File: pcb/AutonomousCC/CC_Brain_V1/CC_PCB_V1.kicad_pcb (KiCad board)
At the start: 2 copper layers, 104.2 x 144.9 mm, 14 parts, among them J1 Screw_Terminal_01x07, J2 Antenna_Conn_02x04_Odd_Even, J3 USB1130-15-A_REVA, J5 Relay_Conn_01x06, U1 Pico, U2 LM337_TO3

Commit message: Added Switch for Pico Programming
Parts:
- added S1: SSA12G, my_footprints:SW_SSA12G, F.Cu at (118.1, 27.9)
- J2: footprint Connector_PinHeader_2.00mm:PinHeader_2x04_P2.00mm_Vertical -> Connector_PinHeader_2.54mm:PinHeader_2x04_P2.54mm_Vertical
- J5: footprint Connector_PinHeader_2.00mm:PinHeader_1x06_P2.00mm_Vertical -> Connector_PinHeader_2.54mm:PinHeader_1x06_P2.54mm_Vertical
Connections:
- U1 pad 39: +3.3V -> +3.3V_Pico
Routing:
- net +3.3V_Pico: track 0.00 -> 30.9 mm
- net +3.3V: track 202.9 -> 190.9 mm
- removed copper zone on B.Cu, net GND
- removed copper zone on F.Cu, net GND

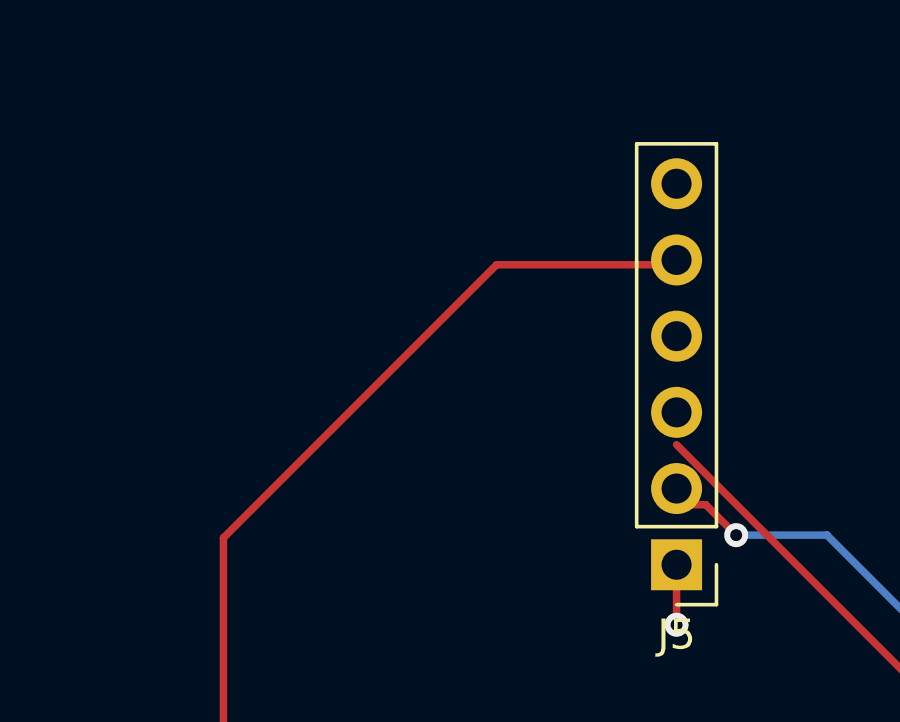
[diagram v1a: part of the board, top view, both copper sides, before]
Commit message: Updated Antenna CC_Brain Pins and Added Relay Circuit
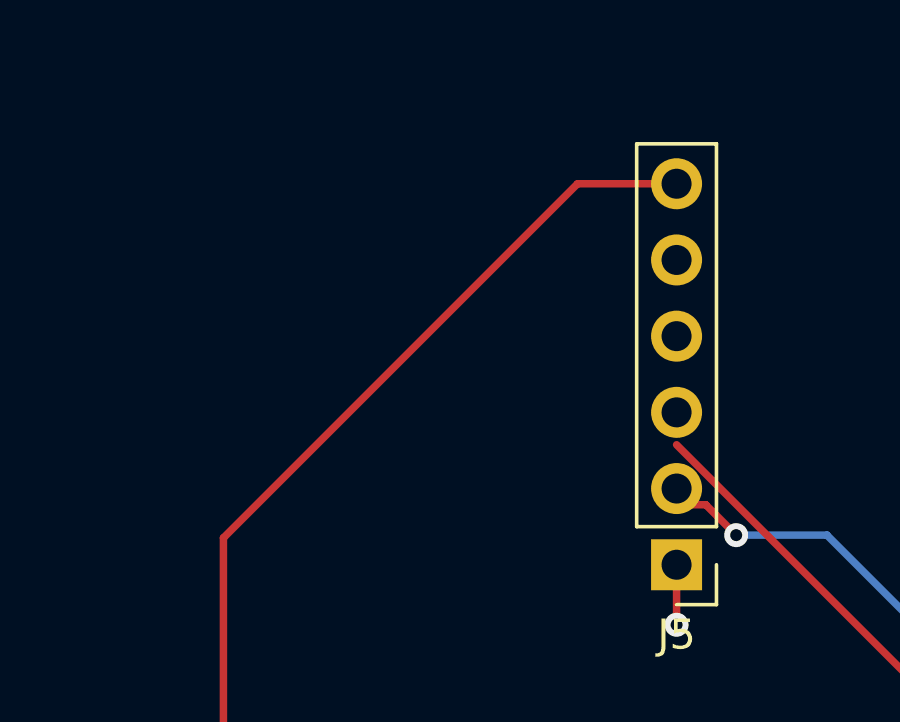
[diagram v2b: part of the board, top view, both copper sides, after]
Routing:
- net +5V: track 163.4 -> 164.6 mm

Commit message: Added most of the footprints
Still need Diodes, Resistors (if THT or SMD), and LED footprints
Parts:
- removed S1: SSA12G, my_footprints:SW_SSA12G
- added J4: Conn_01x02_Male, Connector_PinHeader_2.54mm:PinHeader_1x02_P2.54mm_Vertical, F.Cu at (234.3, 27.4)
- added J6: Conn_01x02_Male, Connector_PinHeader_2.54mm:PinHeader_1x02_P2.54mm_Vertical, F.Cu at (234.3, 34.6)
- added J7: Linear Actuator Power, MCU_RaspberryPi_and_Boards:TE_282837-2, F.Cu at (177.6, 57.9)
- added J8: Linear Actuator, MCU_RaspberryPi_and_Boards:TE_282837-2, F.Cu at (189.3, 57.9)
- added J9: Conn_01x02_Male, Connector_PinHeader_2.54mm:PinHeader_1x02_P2.54mm_Vertical, F.Cu at (245.8, 27.4)
- added K1: FINDER-40.11, Relay_THT:Relay_SPDT_Finder_40.11, F.Cu at (175.5, 29.2)
- added K2: FINDER-40.11, Relay_THT:Relay_SPDT_Finder_40.11, F.Cu at (205.6, 29.2)
- added Q1: PC817A, MCU_RaspberryPi_and_Boards:DIP762W50P254L650H458Q4B, F.Cu at (200.9, 56.3)
- added Q2: PC817A, MCU_RaspberryPi_and_Boards:DIP762W50P254L650H458Q4B, F.Cu at (211.9, 56.3)
- added Q3: BC547A, Package_TO_SOT_THT:TO-92_Inline, F.Cu at (219.1, 56.3)
- added Q4: BC547A, Package_TO_SOT_THT:TO-92_Inline, F.Cu at (234.0, 42.7)
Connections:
- J2 pad 6: GP4 -> GP7
- J2 pad 7: GP7 -> GP4

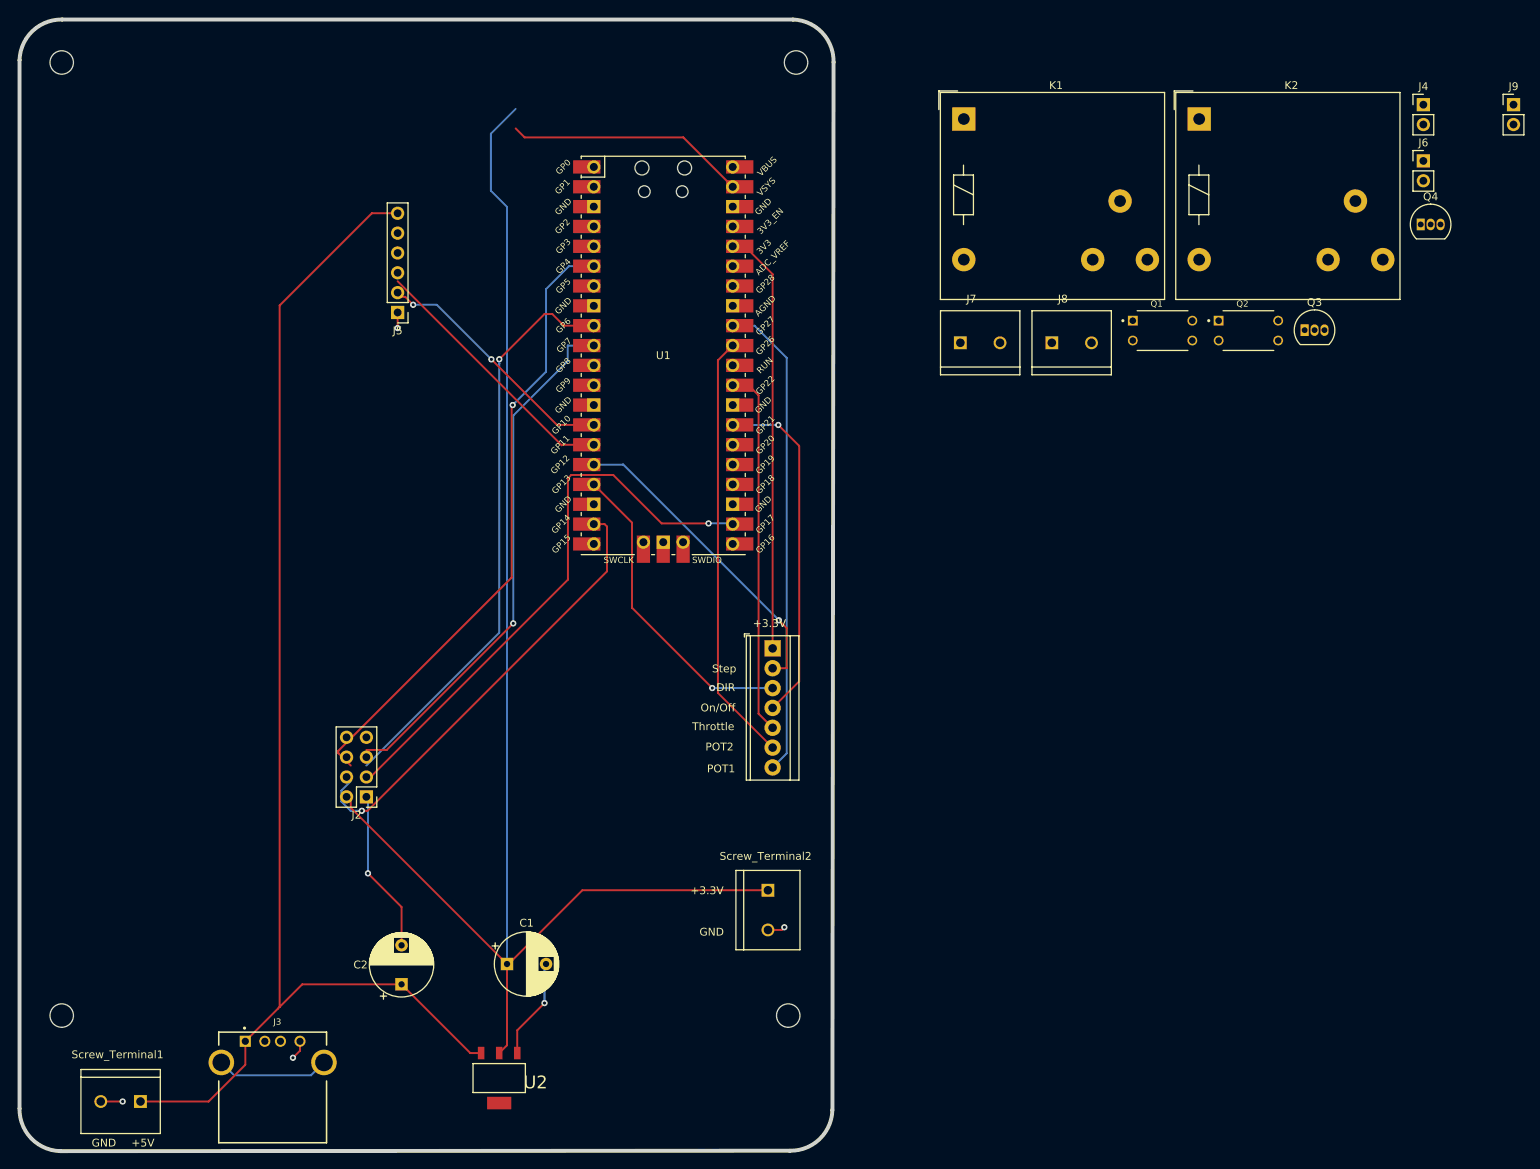
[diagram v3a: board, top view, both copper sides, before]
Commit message: Updated Footprints and PCB Layout
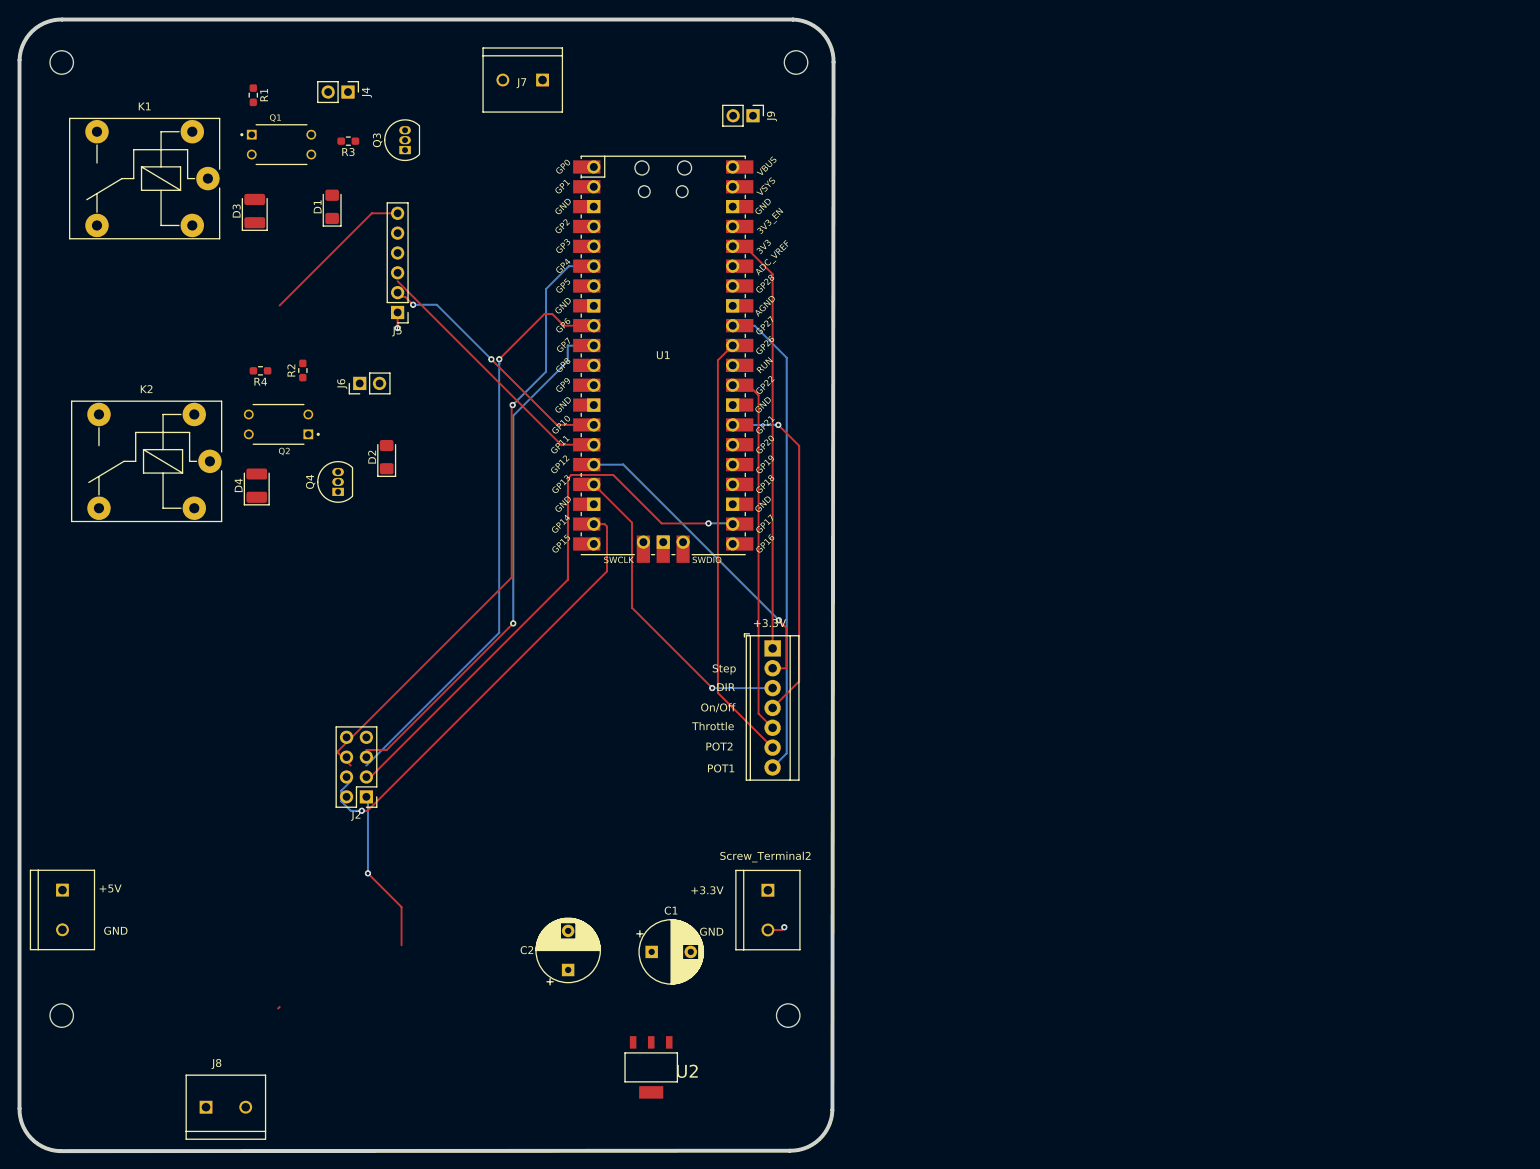
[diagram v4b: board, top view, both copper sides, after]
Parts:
- removed J3: USB1130-15-A_REVA, MCU_RaspberryPi_and_Boards:GCT_USB1130-15-A_REVA
- added D1: SMD LED1, LED_SMD:LED_1206_3216Metric_Pad1.42x1.75mm_HandSolder, F.Cu at (94.6, 40.5)
- added D2: SMD LED2, LED_SMD:LED_1206_3216Metric_Pad1.42x1.75mm_HandSolder, F.Cu at (101.6, 72.5)
- added D3: DIODE, Diode_SMD:D_1210_3225Metric_Pad1.42x2.65mm_HandSolder, F.Cu at (84.7, 41.0)
- added D4: DIODE, Diode_SMD:D_1210_3225Metric_Pad1.42x2.65mm_HandSolder, F.Cu at (85.0, 76.2)
- added R1: 1k, Resistor_SMD:R_0603_1608Metric_Pad0.98x0.95mm_HandSolder, F.Cu at (84.5, 26.2)
- added R2: 1k, Resistor_SMD:R_0603_1608Metric_Pad0.98x0.95mm_HandSolder, F.Cu at (90.9, 61.4)
- added R3: 1k, Resistor_SMD:R_0603_1608Metric_Pad0.98x0.95mm_HandSolder, F.Cu at (96.7, 32.1)
- added R4: 1k, Resistor_SMD:R_0603_1608Metric_Pad0.98x0.95mm_HandSolder, F.Cu at (85.4, 61.5)
- K1, K2: footprint Relay_THT:Relay_SPDT_Finder_40.11 -> Relay_THT:Relay_SPDT_Finder_36.11
- moved J8 145.9 mm to (81.0, 155.7)
- moved Q4 142.7 mm to (95.4, 77.0), turned to 90 degrees
- moved J6 139.1 mm to (98.1, 63.1), turned to 90 degrees
- moved J4 137.7 mm to (96.6, 25.8), turned to 270 degrees
- moved K2 134.0 mm to (79.0, 73.1), turned to 180 degrees
- moved Q2 124.7 mm to (87.8, 68.3), turned to 180 degrees
- moved Q3 117.4 mm to (103.9, 33.2), turned to 90 degrees
- moved Q1 115.3 mm to (88.1, 32.5)
- moved J9 97.4 mm to (148.5, 28.8), turned to 270 degrees
- moved K1 97.1 mm to (78.7, 36.9), turned to 180 degrees
- moved J7 67.5 mm to (119.0, 24.2), turned to 180 degrees
- moved Screw_Terminal1 25.6 mm to (60.1, 130.5), turned to 270 degrees
- moved C2 21.4 mm to (124.8, 138.2)
- moved U2 19.5 mm to (135.5, 150.6)
- moved C1 18.6 mm to (135.5, 135.9)
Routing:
- net +3.3V: track 190.9 -> 0.00 mm
- net +5V: track 164.6 -> 20.3 mm
- net +3.3V_Pico: track 30.9 -> 0.00 mm
- net GND: track 42.9 -> 25.1 mm, vias 6 -> 3
- net Net-(J3-PadS1): track 14.5 -> 0.00 mm

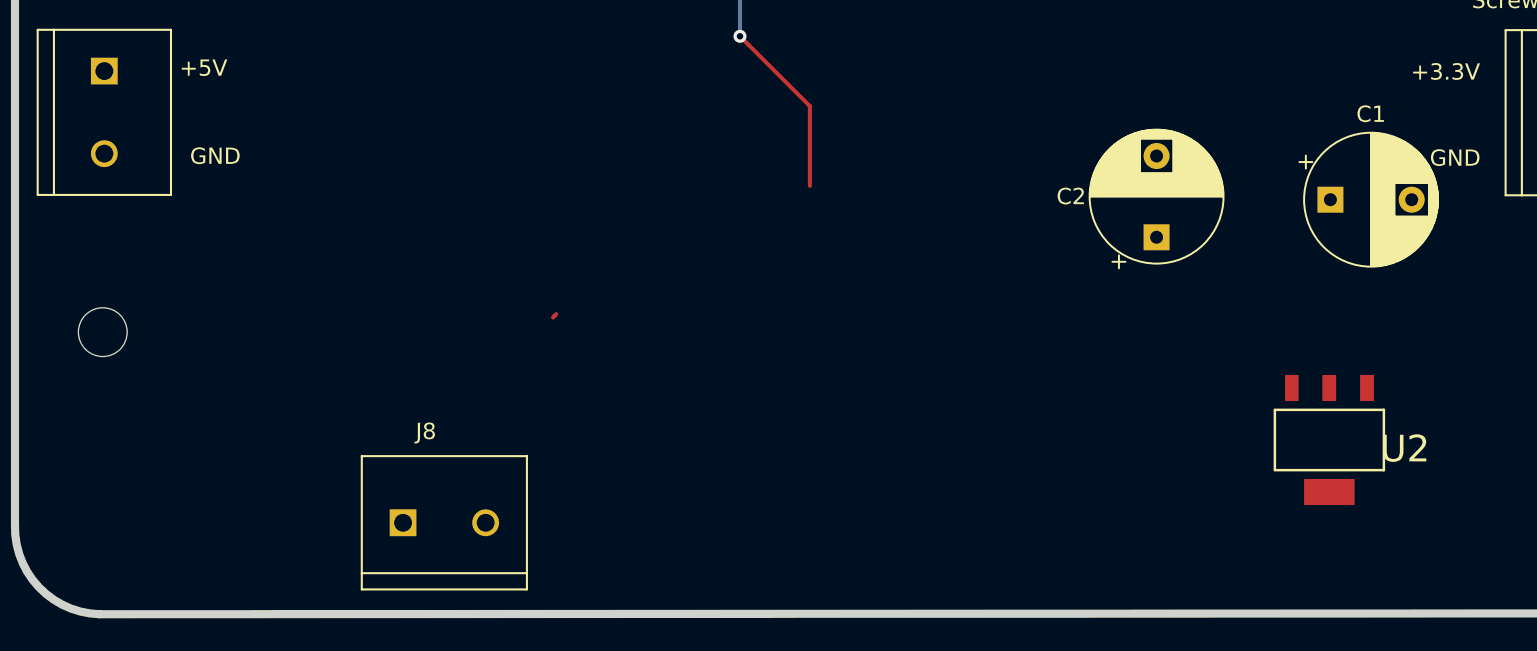
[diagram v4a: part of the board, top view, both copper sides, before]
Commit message: Updated Footprint and Fixed PCB Layout
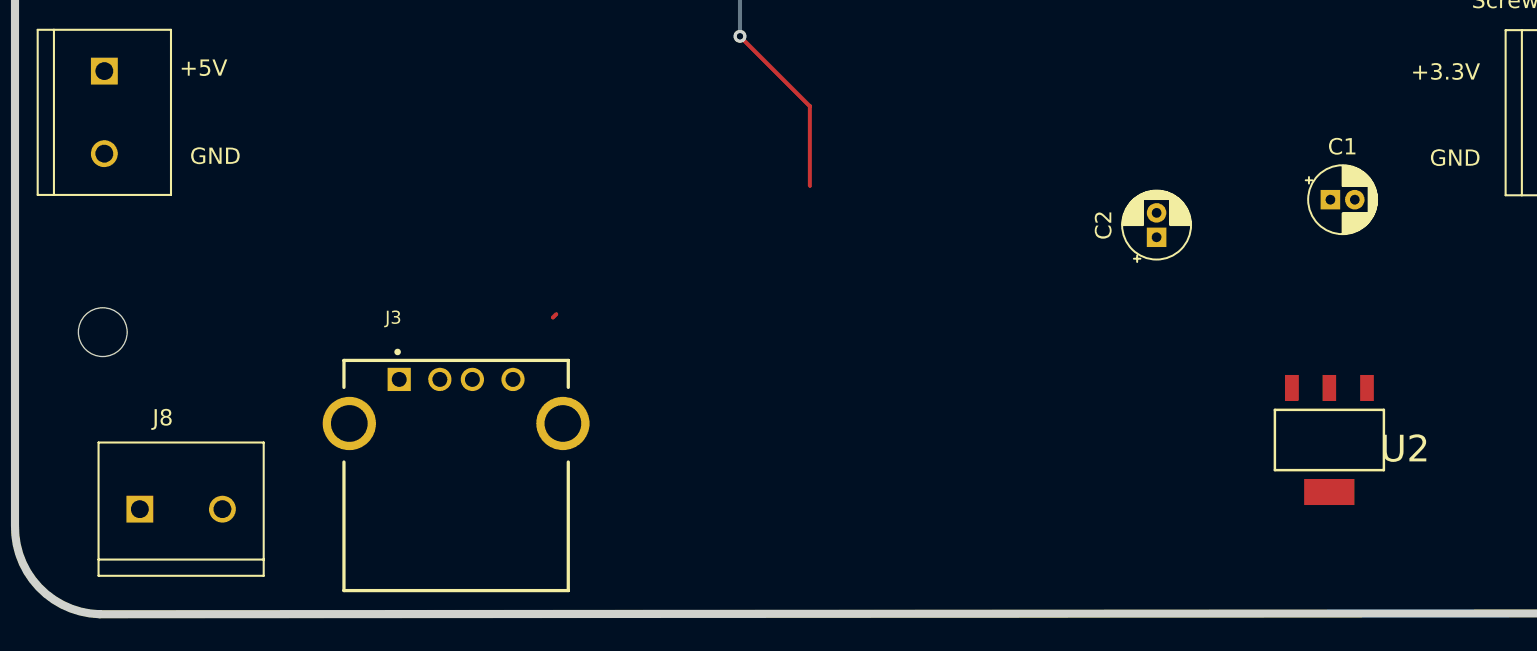
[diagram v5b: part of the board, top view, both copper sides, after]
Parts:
- added J3: USB1130-15-A_REVA, MCU_RaspberryPi_and_Boards:GCT_USB1130-15-A_REVA, F.Cu at (81.7, 149.6)
- C1, C2: footprint Capacitor_THT:CP_Radial_D8.0mm_P5.00mm -> Capacitor_THT:CP_Radial_D4.0mm_P1.50mm
- moved J8 16.2 mm to (64.8, 154.9)
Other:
- board text added: "Autonomous Crazy Cart V1.1"
- board text removed: "Autonomous Crazy Cart V1"
